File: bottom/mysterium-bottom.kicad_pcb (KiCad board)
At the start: 2 copper layers, 347.7 x 146.6 mm, 22 parts

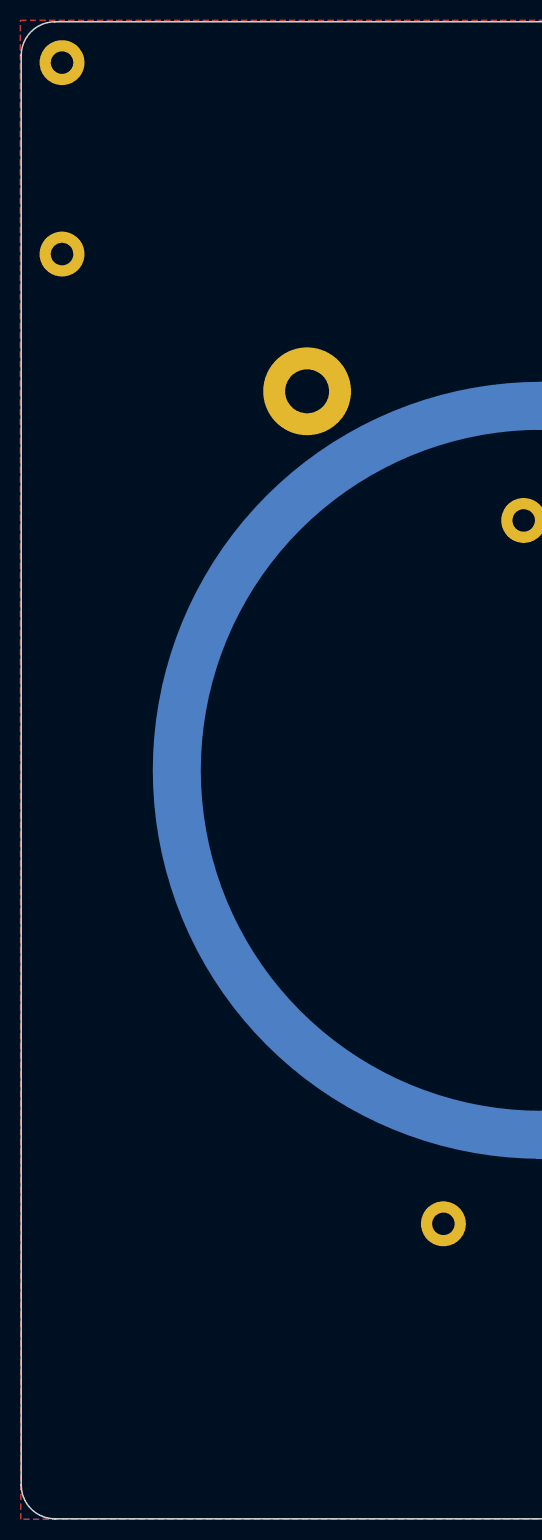
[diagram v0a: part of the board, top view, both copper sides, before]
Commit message: Add split backspace support
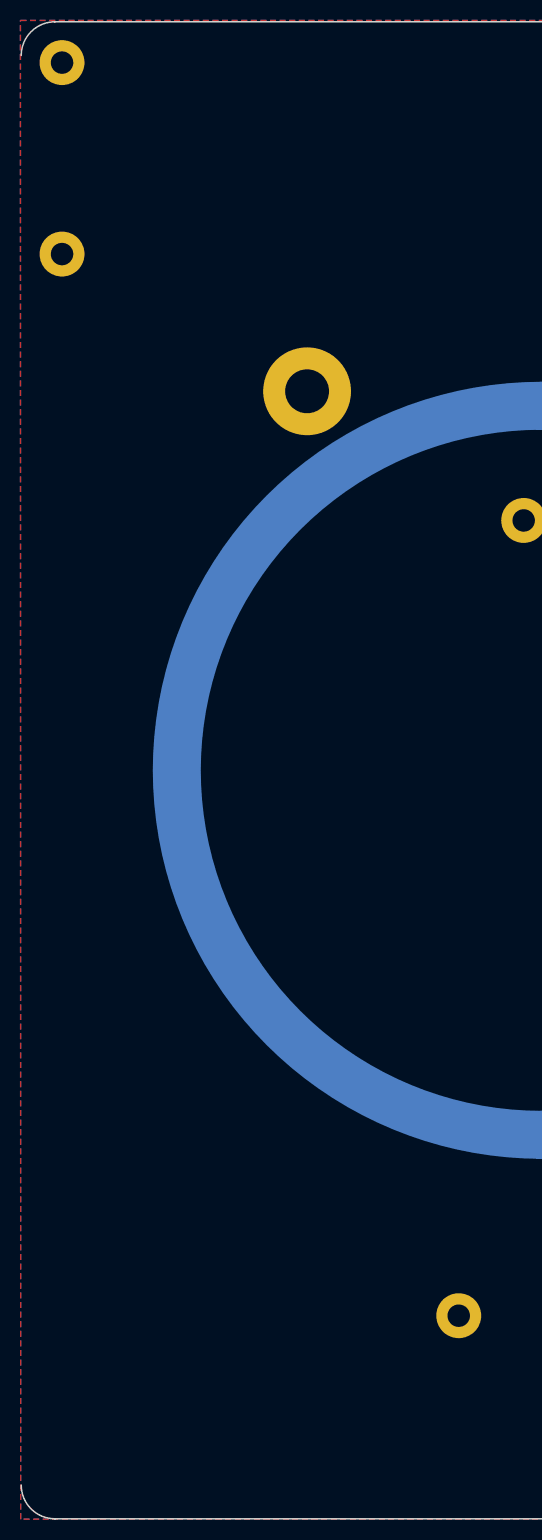
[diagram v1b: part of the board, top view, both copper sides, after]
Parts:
- moved REF** 9.12 mm to (79.4, 187.6)

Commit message: Add support for 0.91" 128x32 OLED display
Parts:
- removed the REF** at (328.0, 155.2)
- removed the REF** at (379.5, 183.5)
- removed the REF** at (328.0, 183.5)
- moved REF** 35.4 mm to (365.2, 187.6)
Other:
- board text added: "JLCJLCJLCJLC"
